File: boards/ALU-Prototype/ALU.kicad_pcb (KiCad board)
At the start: 2 copper layers, 69.2 x 57.2 mm, 60 parts, among them U01 7400, U02 7400, U03 7400, U04 7400, U11 7400, U12 7400, U13 7400, U14 7400, U21 7400, U22 7400, U23 7400, U24 7400, U31 7400, U32 7400, U33 7400, U34 7400

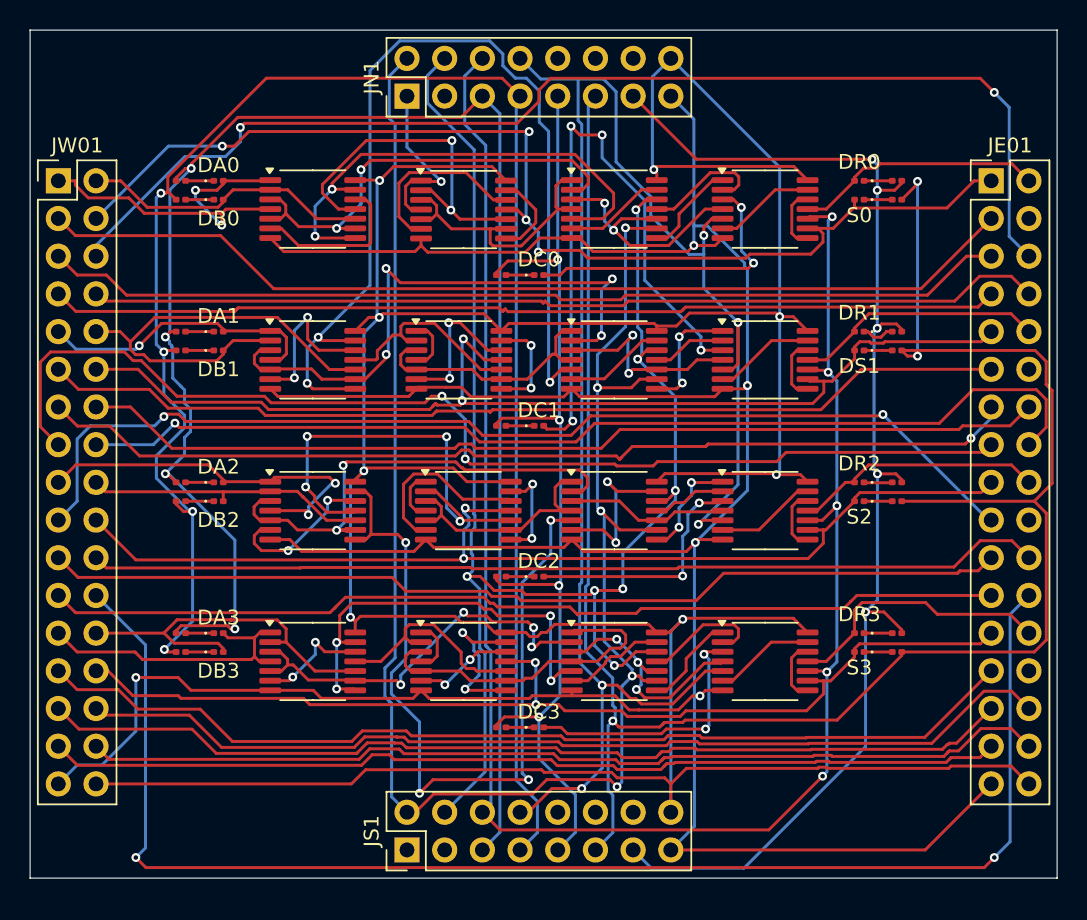
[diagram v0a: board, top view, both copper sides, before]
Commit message: Routing complete. Corrected some errors
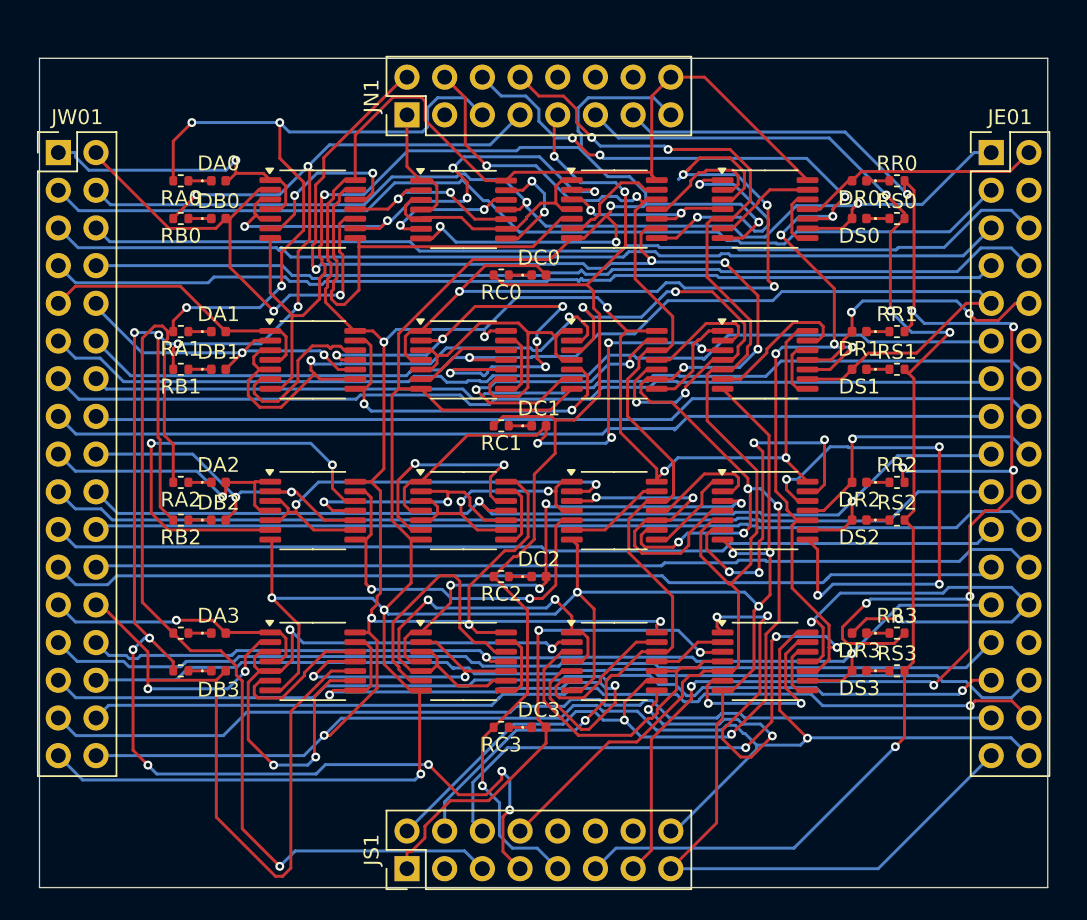
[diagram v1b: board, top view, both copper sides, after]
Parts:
- DA0, DA1, DA2, DA3, DB0, DB1, DB2, DB3, DC0, DC1, DC2, DC3, DR0, DR1, DR2, DR3, DS1: value LED -> ~; footprint LED_SMD:LED_0201_0603Metric -> LED_SMD:LED_0402_1005Metric
- DS0: renamed from S0; value LED -> ~; footprint LED_SMD:LED_0201_0603Metric -> LED_SMD:LED_0402_1005Metric
- DS2: renamed from S2; value LED -> ~; footprint LED_SMD:LED_0201_0603Metric -> LED_SMD:LED_0402_1005Metric
- DS3: renamed from S3; value LED -> ~; footprint LED_SMD:LED_0201_0603Metric -> LED_SMD:LED_0402_1005Metric
- JE01, JW01: value Conn_02x17_Odd_Even -> ~
- JN1, JS1: value Conn_02x08_Odd_Even -> ~
- RA0, RA1, RA2, RA3, RB0, RB1, RB2, RB3, RC0, RC1, RC2, RC3, RR0, RR1, RR2, RR3, RS0, RS1, RS2, RS3: value R -> 330; footprint Resistor_SMD:R_0201_0603Metric -> Resistor_SMD:R_0402_1005Metric
- U01, U02, U03, U04, U11, U12, U13, U14, U21, U22, U23, U24, U31, U32, U33, U34: value 7400 -> ~
- moved JE01 1.91 mm to (147.3, 47.0)
- moved JW01 1.91 mm to (84.5, 47.0)
- moved DB3 1.27 mm to (95.2, 81.9)
- moved DS3 1.27 mm to (138.4, 81.9)
- moved RB3 1.27 mm to (92.7, 81.9)
- moved RS3 1.27 mm to (141.0, 81.9)
- moved DB0 1.27 mm to (95.2, 51.4)
- moved DS0 1.27 mm to (138.4, 51.4)
- moved RB0 1.27 mm to (92.7, 51.4)
- moved RS0 1.27 mm to (141.0, 51.4)
- moved DB1 1.27 mm to (95.2, 61.6)
- moved DB2 1.27 mm to (95.2, 71.8)
- moved DS1 1.27 mm to (138.4, 61.6)
- moved DS2 1.27 mm to (138.4, 71.8)
- moved RB1 1.27 mm to (92.7, 61.6)
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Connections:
- DC3 pad 2: /ALUSlice3/C -> C
- U12 pad 1: /ALUSlice1/Cin -> /ALUSlice0/C
- U12 pad 4: /ALUSlice1/Cin -> /ALUSlice0/C
- U22 pad 1: /ALUSlice2/Cin -> /ALUSlice1/C
- U22 pad 4: /ALUSlice2/Cin -> /ALUSlice1/C
- U32 pad 1: /ALUSlice3/Cin -> /ALUSlice2/C
- U32 pad 4: /ALUSlice3/Cin -> /ALUSlice2/C
- U34 pad 3: /ALUSlice3/C -> C
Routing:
- net GND: track 231.7 -> 299.1 mm, vias 5 -> 12
- net GNDS: track 138.7 -> 89.4 mm, vias 3 -> 4
- net Net-(U11-Pad13): track 64.7 -> 24.2 mm, vias 3 -> 2
- net /ALUSlice0/C: track 20.1 -> 59.4 mm, vias 2 -> 4
- net C: track 0.00 -> 34.9 mm, vias 0 -> 2
- net GNDR: track 86.9 -> 120.6 mm, vias 5 -> 9
- net PE2: track 96.3 -> 64.1 mm, vias 2 -> 0
- net Net-(U24-Pad12): track 4.25 -> 35.5 mm, vias 0 -> 4
- net B3: track 25.6 -> 55.1 mm, vias 0 -> 2
- net SUB: track 107.8 -> 80.4 mm, vias 7 -> 3
- net Net-(U21-Pad13): track 53.2 -> 26.7 mm, vias 4 -> 2
- net Net-(U33-Pad8): track 6.53 -> 29.5 mm, vias 0 -> 4
- net Net-(U11-Pad11): track 14.0 -> 35.2 mm, vias 0 -> 6
- net AND: track 114.3 -> 93.4 mm, vias 5 -> 2
- net Net-(U21-Pad12): track 10.6 -> 29.5 mm
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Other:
- board size 69.2 x 57.2 mm -> 67.9 x 55.9 mm

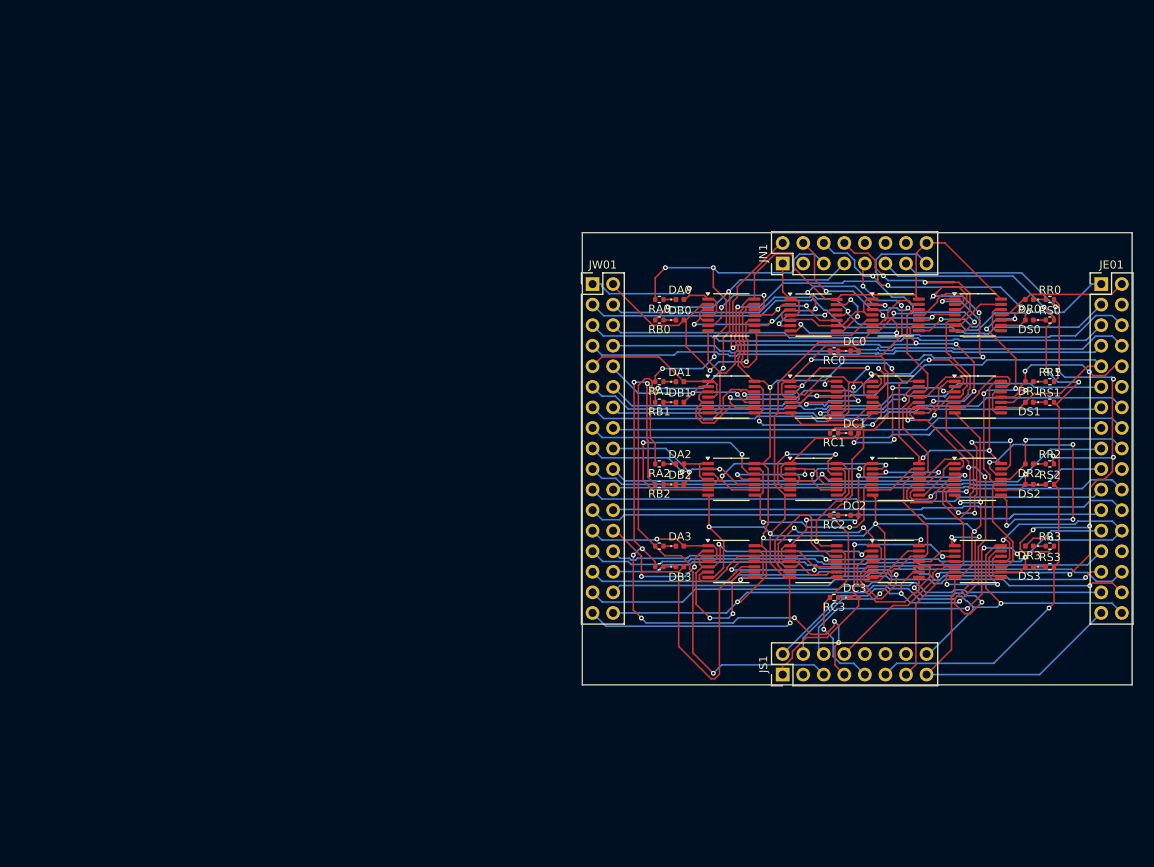
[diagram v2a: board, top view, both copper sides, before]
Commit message: ^Move origin. Lines between all slices
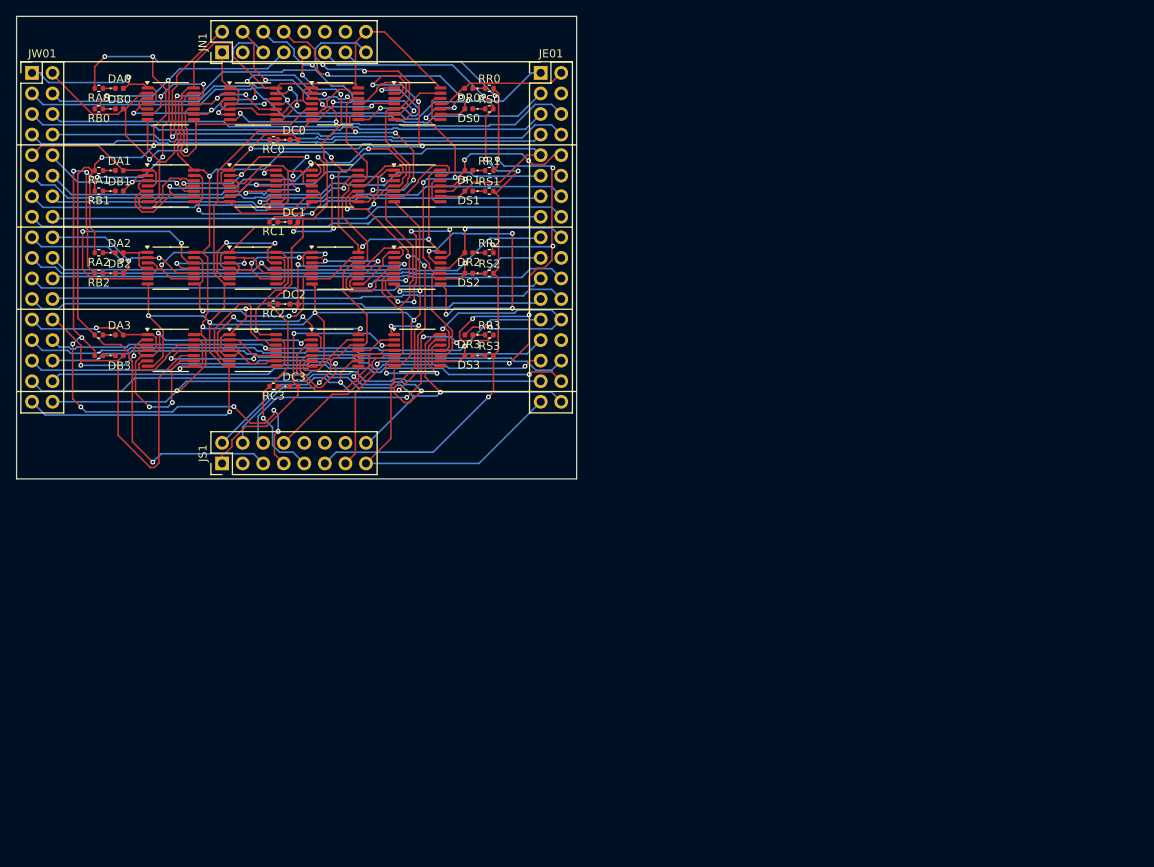
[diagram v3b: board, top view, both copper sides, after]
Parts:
- moved U04 74.0 mm to (62.8, 24.7)
- moved U14 74.0 mm to (62.8, 34.9)
- moved U24 74.0 mm to (62.8, 45.0)
- moved U34 74.0 mm to (62.8, 55.2)
- moved DC0 74.0 mm to (47.6, 29.2)
- moved DC1 74.0 mm to (47.6, 39.3)
- moved DC2 74.0 mm to (47.6, 49.5)
- moved DC3 74.0 mm to (47.6, 59.6)
- moved DR0 74.0 mm to (69.2, 22.8)
- moved DR1 74.0 mm to (69.2, 33.0)
- moved DR2 74.0 mm to (69.2, 43.1)
- moved DR3 74.0 mm to (69.2, 53.3)
- moved DS0 74.0 mm to (69.2, 25.3)
- moved DS1 74.0 mm to (69.2, 35.5)
- moved DS2 74.0 mm to (69.2, 45.7)
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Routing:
- net AND: track 93.4 -> 86.2 mm
- net /ALUSlice0/C: track 59.4 -> 55.9 mm
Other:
- board size 67.9 x 55.9 mm -> 69.2 x 57.2 mm

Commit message: 8-bit PCB, P1 version
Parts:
- added DA4: ~, LED_SMD:LED_0402_1005Metric, F.Cu at (29.8, 71.8)
- added DA5: ~, LED_SMD:LED_0402_1005Metric, F.Cu at (29.8, 81.9)
- added DA6: ~, LED_SMD:LED_0402_1005Metric, F.Cu at (29.8, 92.1)
- added DA7: ~, LED_SMD:LED_0402_1005Metric, F.Cu at (29.8, 102.2)
- added DB4: ~, LED_SMD:LED_0402_1005Metric, F.Cu at (29.8, 74.3)
- added DB5: ~, LED_SMD:LED_0402_1005Metric, F.Cu at (29.8, 84.5)
- added DB6: ~, LED_SMD:LED_0402_1005Metric, F.Cu at (29.8, 94.6)
- added DB7: ~, LED_SMD:LED_0402_1005Metric, F.Cu at (29.8, 104.8)
- added DC4: ~, LED_SMD:LED_0402_1005Metric, F.Cu at (51.4, 78.1)
- added DC5: ~, LED_SMD:LED_0402_1005Metric, F.Cu at (51.4, 88.3)
- added DC6: ~, LED_SMD:LED_0402_1005Metric, F.Cu at (51.4, 98.4)
- added DC7: ~, LED_SMD:LED_0402_1005Metric, F.Cu at (51.4, 108.6)
- added DR4: ~, LED_SMD:LED_0402_1005Metric, F.Cu at (73.0, 71.8)
- added DR5: ~, LED_SMD:LED_0402_1005Metric, F.Cu at (73.0, 81.9)
- added DR6: ~, LED_SMD:LED_0402_1005Metric, F.Cu at (73.0, 92.1)
- added DR7: ~, LED_SMD:LED_0402_1005Metric, F.Cu at (73.0, 102.2)
- added DS4: ~, LED_SMD:LED_0402_1005Metric, F.Cu at (73.0, 74.3)
- added DS5: ~, LED_SMD:LED_0402_1005Metric, F.Cu at (73.0, 84.5)
- added DS6: ~, LED_SMD:LED_0402_1005Metric, F.Cu at (73.0, 94.6)
- added DS7: ~, LED_SMD:LED_0402_1005Metric, F.Cu at (73.0, 104.8)
- added JE47: ~, Connector_PinHeader_2.54mm:PinHeader_2x17_P2.54mm_Vertical, F.Cu at (81.9, 69.9)
- added JW47: ~, Connector_PinHeader_2.54mm:PinHeader_2x17_P2.54mm_Vertical, F.Cu at (19.1, 69.9)
- added RA4: 330, Resistor_SMD:R_0402_1005Metric, F.Cu at (27.3, 71.8)
- added RA5: 330, Resistor_SMD:R_0402_1005Metric, F.Cu at (27.3, 81.9)
- added RA6: 330, Resistor_SMD:R_0402_1005Metric, F.Cu at (27.3, 92.1)
- added RA7: 330, Resistor_SMD:R_0402_1005Metric, F.Cu at (27.3, 102.2)
- added RB4: 330, Resistor_SMD:R_0402_1005Metric, F.Cu at (27.3, 74.3)
- added RB5: 330, Resistor_SMD:R_0402_1005Metric, F.Cu at (27.3, 84.5)
- added RB6: 330, Resistor_SMD:R_0402_1005Metric, F.Cu at (27.3, 94.6)
- added RB7: 330, Resistor_SMD:R_0402_1005Metric, F.Cu at (27.3, 104.8)
- added RC4: 330, Resistor_SMD:R_0402_1005Metric, F.Cu at (48.9, 78.1)
- added RC5: 330, Resistor_SMD:R_0402_1005Metric, F.Cu at (48.9, 88.3)
- added RC6: 330, Resistor_SMD:R_0402_1005Metric, F.Cu at (48.9, 98.4)
- added RC7: 330, Resistor_SMD:R_0402_1005Metric, F.Cu at (48.9, 108.6)
- added RR4: 330, Resistor_SMD:R_0402_1005Metric, F.Cu at (75.6, 71.8)
- added RR5: 330, Resistor_SMD:R_0402_1005Metric, F.Cu at (75.6, 81.9)
- added RR6: 330, Resistor_SMD:R_0402_1005Metric, F.Cu at (75.6, 92.1)
- added RR7: 330, Resistor_SMD:R_0402_1005Metric, F.Cu at (75.6, 102.2)
- added RS4: 330, Resistor_SMD:R_0402_1005Metric, F.Cu at (75.6, 74.3)
- added RS5: 330, Resistor_SMD:R_0402_1005Metric, F.Cu at (75.6, 84.5)
- added RS6: 330, Resistor_SMD:R_0402_1005Metric, F.Cu at (75.6, 94.6)
- added RS7: 330, Resistor_SMD:R_0402_1005Metric, F.Cu at (75.6, 104.8)
- added U41: ~, Package_SO:TSSOP-14_4.4x5mm_P0.65mm, F.Cu at (36.2, 73.7)
- added U42: ~, Package_SO:TSSOP-14_4.4x5mm_P0.65mm, F.Cu at (46.4, 73.7)
- added U43: ~, Package_SO:TSSOP-14_4.4x5mm_P0.65mm, F.Cu at (56.5, 73.7)
- added U44: ~, Package_SO:TSSOP-14_4.4x5mm_P0.65mm, F.Cu at (66.7, 73.7)
- added U51: ~, Package_SO:TSSOP-14_4.4x5mm_P0.65mm, F.Cu at (36.2, 83.8)
- added U52: ~, Package_SO:TSSOP-14_4.4x5mm_P0.65mm, F.Cu at (46.4, 83.8)
- added U53: ~, Package_SO:TSSOP-14_4.4x5mm_P0.65mm, F.Cu at (56.5, 83.8)
- added U54: ~, Package_SO:TSSOP-14_4.4x5mm_P0.65mm, F.Cu at (66.7, 83.8)
- added U61: ~, Package_SO:TSSOP-14_4.4x5mm_P0.65mm, F.Cu at (36.2, 94.0)
- added U62: ~, Package_SO:TSSOP-14_4.4x5mm_P0.65mm, F.Cu at (46.4, 94.0)
- added U63: ~, Package_SO:TSSOP-14_4.4x5mm_P0.65mm, F.Cu at (56.5, 94.0)
- added U64: ~, Package_SO:TSSOP-14_4.4x5mm_P0.65mm, F.Cu at (66.7, 94.0)
- added U71: ~, Package_SO:TSSOP-14_4.4x5mm_P0.65mm, F.Cu at (36.2, 104.1)
- added U72: ~, Package_SO:TSSOP-14_4.4x5mm_P0.65mm, F.Cu at (46.4, 104.1)
- added U73: ~, Package_SO:TSSOP-14_4.4x5mm_P0.65mm, F.Cu at (56.5, 104.1)
- added U74: ~, Package_SO:TSSOP-14_4.4x5mm_P0.65mm, F.Cu at (66.7, 104.1)
- moved JS1 46.6 mm to (42.5, 115.6)
- moved RR2 5.04 mm to (75.6, 46.4)
- moved RS1 5.04 mm to (75.6, 38.7)
- moved RS3 5.04 mm to (75.6, 59.1)
- moved RR0 5.04 mm to (75.6, 26.0)
- moved RS0 5.04 mm to (75.6, 28.6)
- moved RR1 5.04 mm to (75.6, 36.2)
- moved RR3 5.04 mm to (75.6, 56.5)
- moved RS2 5.04 mm to (75.6, 48.9)
- moved DC0 5.04 mm to (51.4, 32.4)
- moved DC2 5.04 mm to (51.4, 52.7)
- moved RA2 5.04 mm to (27.3, 46.4)
- moved RB1 5.04 mm to (27.3, 38.7)
- moved RB3 5.04 mm to (27.3, 59.1)
- moved RC0 5.04 mm to (48.9, 32.4)
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- renumbered JE01 to JE03, JW01 to JW03
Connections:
- DC3 pad 2: C -> /ALUSlice3/C
- U34 pad 3: C -> /ALUSlice3/C
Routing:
- net VDD: track 269.6 -> 536.9 mm, vias 10 -> 25
- net GND: track 299.1 -> 518.3 mm, vias 12 -> 15
- net SUB: track 80.4 -> 213.2 mm, vias 3 -> 9
- net ADD: track 135.5 -> 253.3 mm, vias 11 -> 15
- net XOR: track 114.8 -> 230.5 mm, vias 11 -> 17
- net GNDC: track 75.9 -> 179.1 mm, vias 3 -> 6
- net S5: track 0.00 -> 89.3 mm, vias 0 -> 3
- net S7: track 0.00 -> 86.3 mm, vias 0 -> 2
- net S4: track 0.00 -> 85.5 mm, vias 0 -> 2
- net GNDS: track 89.4 -> 166.7 mm, vias 4 -> 7
- net S6: track 0.00 -> 75.5 mm, vias 0 -> 2
- net PD7: track 0.00 -> 67.6 mm, vias 0 -> 1
- net PB7: track 0.00 -> 66.5 mm
- net PA4: track 0.00 -> 66.4 mm
- net PD5: track 0.00 -> 66.3 mm
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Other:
- board size 69.2 x 57.2 mm -> 67.9 x 99.1 mm
